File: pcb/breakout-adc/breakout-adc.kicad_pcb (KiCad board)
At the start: 4 copper layers, 100 x 62 mm, 107 parts, among them J1 Screw_Terminal_01x04, J10 Conn_01x01_Pin, J11 Conn_01x12_Pin, J12 Conn_01x12_Pin, J13 Conn_01x01_Pin, J14 Conn_01x01_Pin, J15 FX18-120P-0.8SV20, J16 Conn_01x01_Pin, J17 Conn_01x01_Pin, J18 Conn_01x01_Pin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

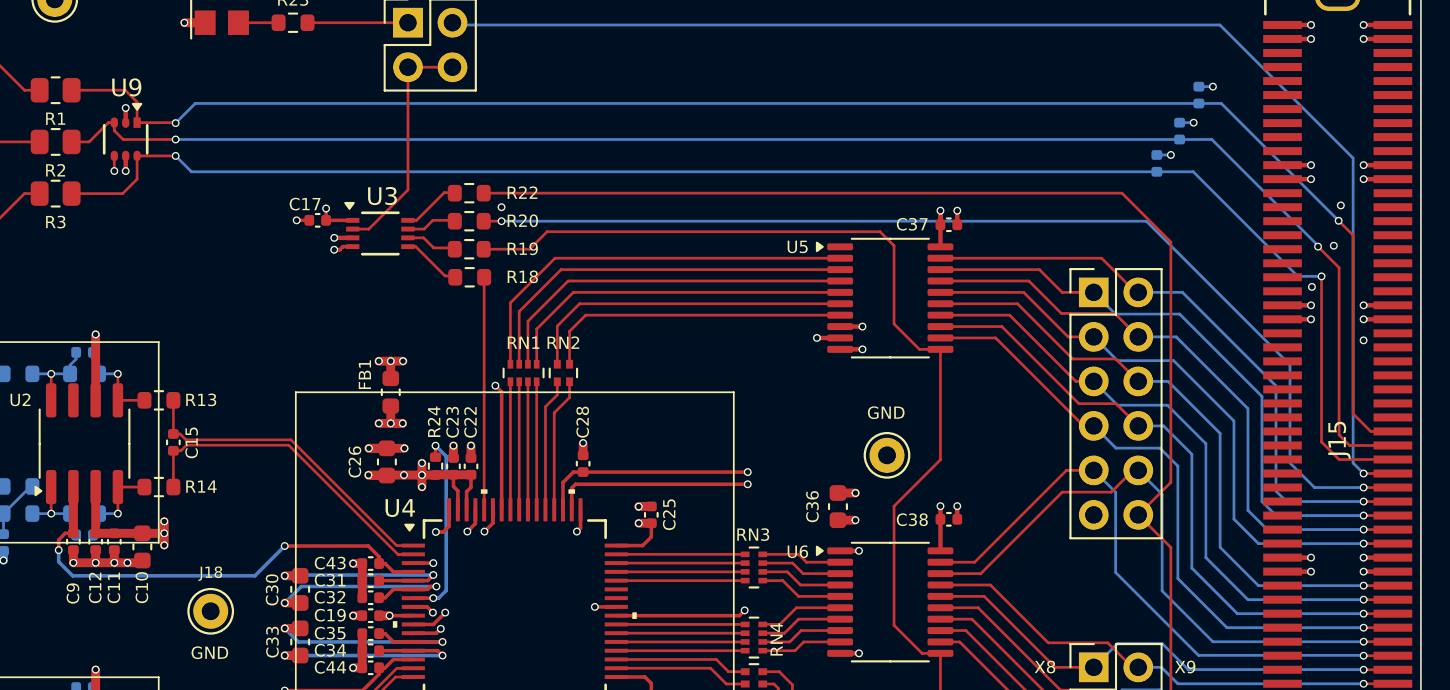
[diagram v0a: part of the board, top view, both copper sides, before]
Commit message: [adc][pcb] silk screen touch ups
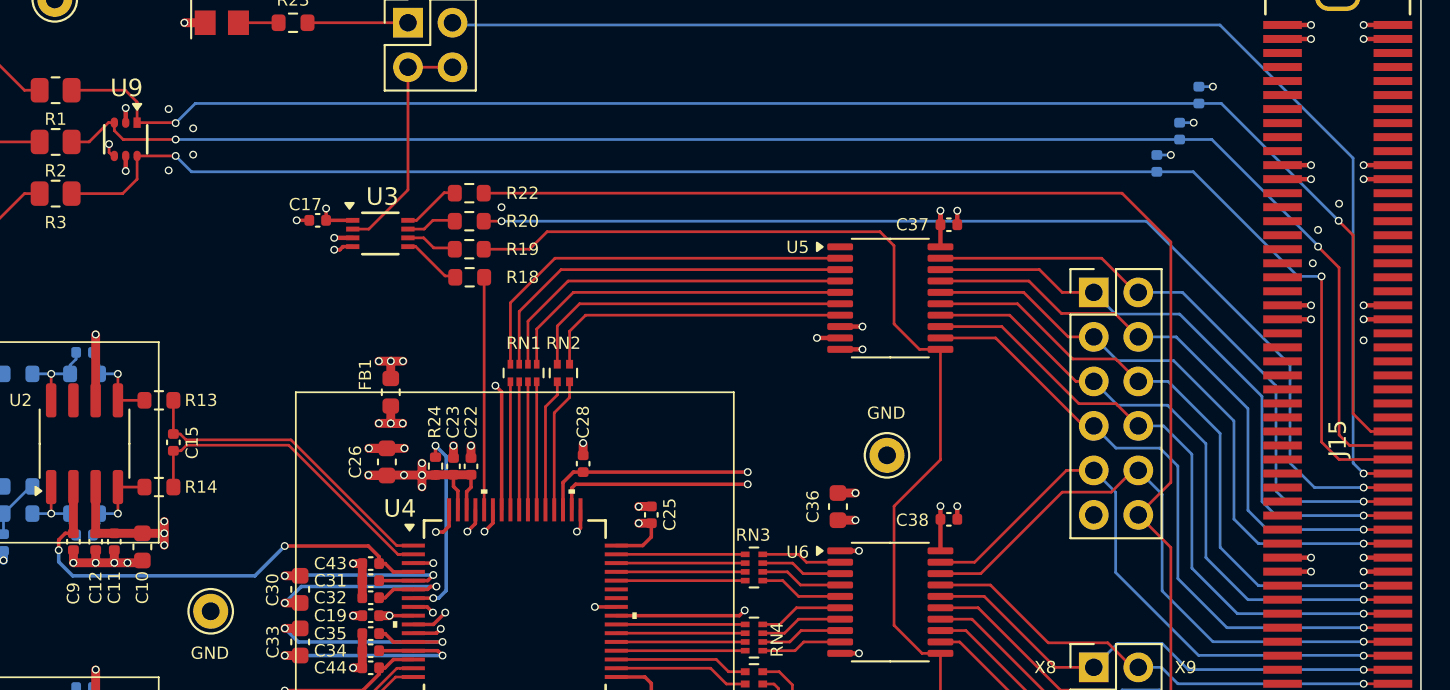
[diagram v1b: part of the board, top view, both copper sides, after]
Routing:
- net GND: track 148.8 -> 148.9 mm, vias 88 -> 92
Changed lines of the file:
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@@
 		)
 		(fp_line
-			(start -1.33 1.270001)
+			(start -1.33 1.27)
 			(end -1.33 14.03)
 			(stroke
@@
 		)
 		(fp_line
-			(start -1.33 1.270001)
+			(start -1.33 1.27)
 			(end 1.27 1.27)
 			(stroke
@@
 		)
 		(fp_line
-			(start 1.27 1.27)
-			(end 1.270001 -1.33)
+			(start 1.27 -1.33)
+			(end 3.87 -1.33)
 			(stroke
 				(width 0.12)
@@
 		)
 		(fp_line
-			(start 1.270001 -1.33)
-			(end 3.87 -1.33)
+			(start 1.27 1.27)
+			(end 1.27 -1.33)
 			(stroke
 				(width 0.12)
@@
 		)
 		(fp_line
-			(start -1.270001 0)
-			(end 0 -1.270001)
+			(start -1.27 0)
+			(end 0 -1.27)
 			(stroke
 				(width 0.1)
@@
 		(fp_line
 			(start -1.27 13.97)
-			(end -1.270001 0)
+			(end -1.27 0)
 			(stroke
 				(width 0.1)
@@
 		)
 		(fp_line
-			(start 0 -1.270001)
+			(start 0 -1.27)
 			(end 3.81 -1.27)
 			(stroke
@@
 		)
 		(pad "5" thru_hole oval
-			(at 0 5.079999)
+			(at 0 5.08)
 			(size 1.7 1.7)
 			(drill 1)
@@
 			(at 0.032 -2.2064 0)
 			(layer "F.SilkS")
+			(hide yes)
 			(effects
 				(font
@@
 		)
 		(fp_line
-			(start -1.33 1.270001)
+			(start -1.33 1.27)
 			(end -1.33 14.03)
 			(stroke
@@
 		)
 		(fp_line
-			(start -1.33 1.270001)
+			(start -1.33 1.27)
 			(end 1.27 1.27)
 			(stroke
@@
 		)
 		(fp_line
-			(start 1.27 1.27)
-			(end 1.270001 -1.33)
+			(start 1.27 -1.33)
+			(end 3.87 -1.33)
 			(stroke
 				(width 0.12)
@@
 		)
 		(fp_line
-			(start 1.270001 -1.33)
-			(end 3.87 -1.33)
+			(start 1.27 1.27)
+			(end 1.27 -1.33)
 			(stroke
 				(width 0.12)
@@
 		)
 		(fp_line
-			(start -1.270001 0)
-			(end 0 -1.270001)
+			(start -1.27 0)
+			(end 0 -1.27)
 			(stroke
 				(width 0.1)
@@
 		(fp_line
 			(start -1.27 13.97)
-			(end -1.270001 0)
+			(end -1.27 0)
 			(stroke
 				(width 0.1)
@@
 		)
 		(fp_line
-			(start 0 -1.270001)
+			(start 0 -1.27)
 			(end 3.81 -1.27)
 			(stroke
@@
 		)
 		(pad "5" thru_hole oval
-			(at 0 5.079999)
+			(at 0 5.08)
 			(size 1.7 1.7)
 			(drill 1)
@@
 	)
 	(segment
-		(start 134.100002 58.775003)
-		(end 134.100002 59.536974)
-		(width 0.156464)
-		(layer "F.Cu")
-		(net 1)
-	)
-	(segment
 		(start 154.456667 94.113025)
 		(end 154.456666 94.113026)
@@
 	)
 	(segment
+		(start 133.8 58)
+		(end 133.8 58.475001)
+		(width 0.156464)
+		(layer "F.Cu")
+		(net 1)
+	)
+	(segment
 		(start 176.55 81.213026)
 		(end 176.6 81.263026)
@@
 	)
 	(segment
+		(start 133.8 58.475001)
+		(end 134.100002 58.775003)
+		(width 0.156464)
+		(layer "F.Cu")
+		(net 1)
+	)
+	(segment
 		(start 152.986469 84.738026)
 		(end 152.311468 85.413027)
@@
 	)
 	(via
-		(at 134.100002 59.536974)
+		(at 133.8 58)
 		(size 0.45)
 		(drill 0.3)
@@
 	)
 	(via
+		(at 137.2 56)
+		(size 0.45)
+		(drill 0.3)
+		(layers "F.Cu" "B.Cu")
+		(net 1)
+	)
+	(via
 		(at 202.4 51.2)
 		(size 0.45)
@@
 	)
 	(via
-		(at 204.1 61.5)
+		(at 204 61.4)
 		(size 0.45)
 		(drill 0.3)
@@
 	)
 	(via
-		(at 202.45 66.15)
+		(at 202.5 64.8)
 		(size 0.45)
 		(drill 0.3)
@@
 	)
 	(via
+		(at 138.6 57.1)
+		(size 0.45)
+		(drill 0.3)
+		(layers "F.Cu" "B.Cu")
+		(net 1)
+	)
+	(via
 		(at 127.775 100.885693)
 		(size 0.45)
@@
 	)
 	(via
+		(at 137.2 59.5)
+		(size 0.45)
+		(drill 0.3)
+		(layers "F.Cu" "B.Cu")
+		(net 1)
+	)
+	(via
 		(at 170.25 91.758223)
 		(size 0.45)
@@
 	)
 	(via
-		(at 203.7 63.8)
+		(at 202.8 62.9)
 		(size 0.45)
 		(drill 0.3)
@@
 		(size 0.45)
 		(drill 0.3)
+		(layers "F.Cu" "B.Cu")
+		(net 1)
+	)
+	(via
+		(at 138.6 58.6)
+		(size 0.45)
+		(drill 0.3)

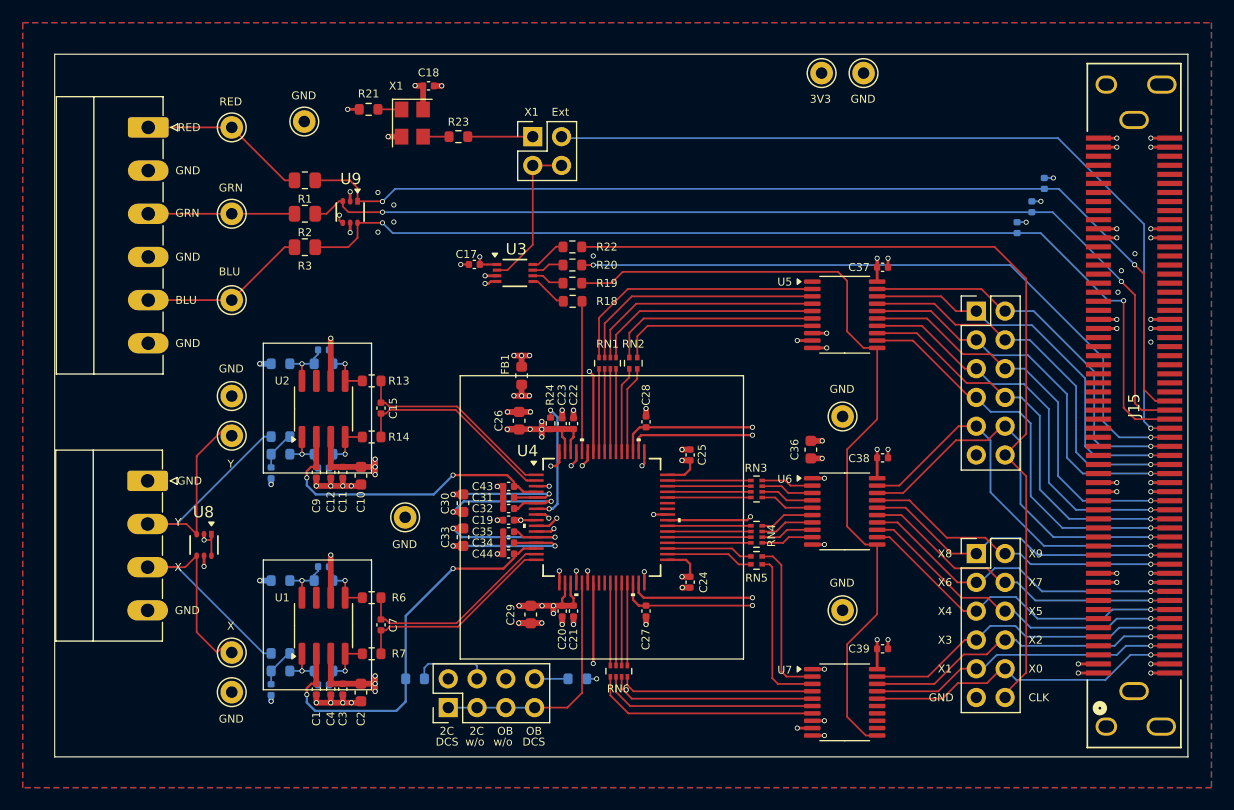
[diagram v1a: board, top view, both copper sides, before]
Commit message: [adc][pcb] add fence vias around pcb
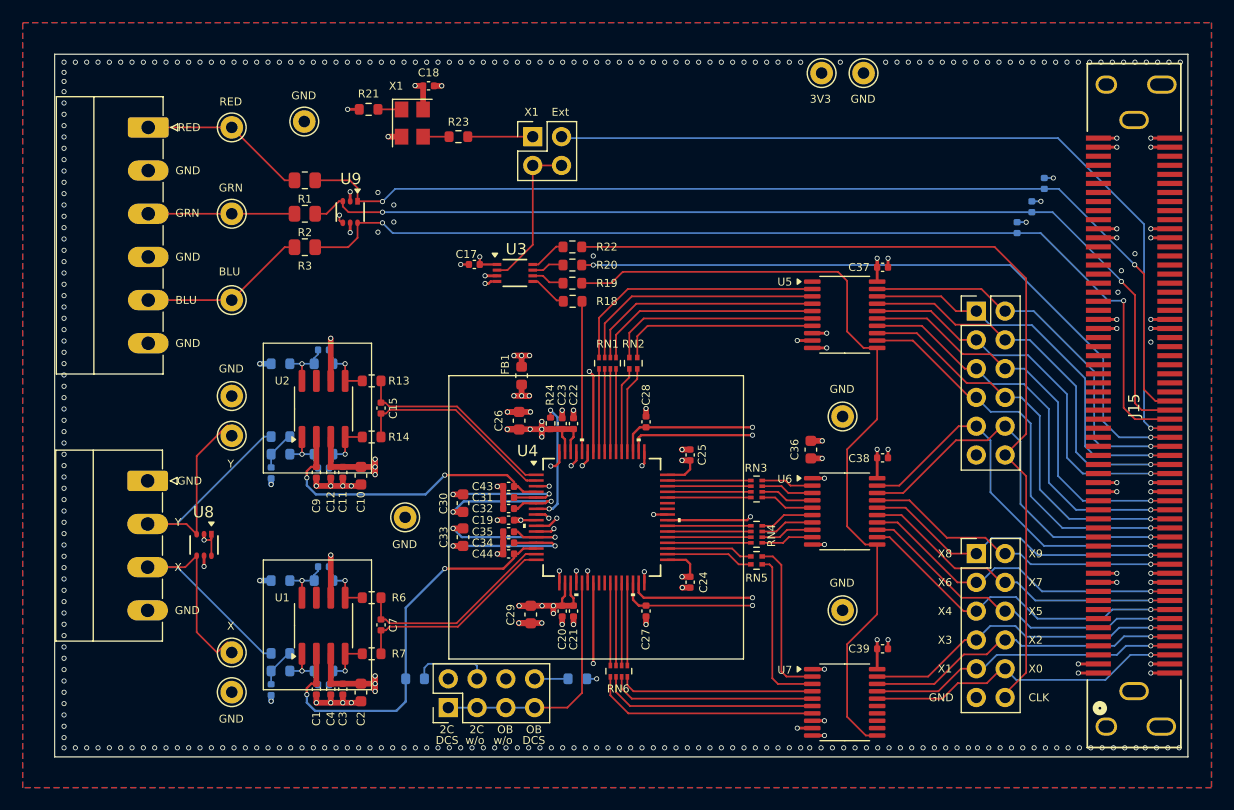
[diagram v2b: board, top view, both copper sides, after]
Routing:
- net GND: vias 92 -> 346

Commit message: [adc][pcb] replace deleted Y hdr silks
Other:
- board text added: "Y0"
- board text added: "Y1"
- board text added: "Y2"
- board text added: "Y3"
- board text added: "Y4"
- board text added: "Y5"
- board text added: "Y6"
- board text added: "Y7"
- board text added: "Y8"
- board text added: "Y9"
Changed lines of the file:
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@@
+		)
+	)
+	(gr_text "Y0"
+		(at 194.6 77.038026 0)
+		(layer "F.SilkS")
+		(effects
+			(font
+				(size 0.7 0.7)
+				(thickness 0.1)
+			)
+			(justify left bottom)
 		)
 	)
@@
 		)
 	)
+	(gr_text "Y7"
+		(at 194.6 69.418026 0)
+		(layer "F.SilkS")
+		(effects
+			(font
+				(size 0.7 0.7)
+				(thickness 0.1)
+			)
+			(justify left bottom)
+		)
+	)
 	(gr_text "Y"
 		(at 119.275 85.513026 0)
@@
 		)
 	)
+	(gr_text "GND"
+		(at 185.8 79.578026 0)
+		(layer "F.SilkS")
+		(effects
+			(font
+				(size 0.7 0.7)
+				(thickness 0.1)
+			)
+			(justify left bottom)
+		)
+	)
 	(gr_text "GRN"
 		(at 123.153334 56 0)
@@
 		)
 	)
+	(gr_text "CLK"
+		(at 194.6 79.578026 0)
+		(layer "F.SilkS")
+		(effects
+			(font
+				(size 0.7 0.7)
+				(thickness 0.1)
+			)
+			(justify left bottom)
+		)
+	)
 	(gr_text "X6"
 		(at 186.599999 90.818026 0)
@@
 		)
 	)
+	(gr_text "Y9"
+		(at 194.6 66.878026 0)
+		(layer "F.SilkS")
+		(effects
+			(font
+				(size 0.7 0.7)
+				(thickness 0.1)
+			)
+			(justify left bottom)
+		)
+	)
 	(gr_text "GND"
 		(at 119.275 93.288026 0)
@@
 		)
 	)
+	(gr_text "Y5"
+		(at 194.6 71.958026 0)
+		(layer "F.SilkS")
+		(effects
+			(font
+				(size 0.7 0.7)
+				(thickness 0.1)
+			)
+			(justify left bottom)
+		)
+	)
 	(gr_text "BLU"
 		(at 123.153334 63.4 0)
@@
 		)
 	)
+	(gr_text "Y4"
+		(at 186.599999 71.958026 0)
+		(layer "F.SilkS")
+		(effects
+			(font
+				(size 0.7 0.7)
+				(thickness 0.1)
+			)
+			(justify left bottom)
+		)
+	)
 	(gr_text "RED"
 		(at 119.5325 50.67 0)
@@
 		)
 	)
+	(gr_text "Y6"
+		(at 186.599999 69.418026 0)
+		(layer "F.SilkS")
+		(effects
+			(font
+				(size 0.7 0.7)
+				(thickness 0.1)
+			)
+			(justify left bottom)
+		)
+	)
 	(gr_text "X5"
 		(at 194.6 93.358026 0)
@@
 		)
 	)
+	(gr_text "Y3"
+		(at 194.6 74.498026 0)
+		(layer "F.SilkS")
+		(effects
+			(font
+				(size 0.7 0.7)
+				(thickness 0.1)
+			)
+			(justify left bottom)
+		)
+	)
 	(gr_text "GND"
 		(at 129.553334 47.863026 0)
@@
 		)
 	)
+	(gr_text "Y2"
+		(at 186.599999 74.498026 0)
+		(layer "F.SilkS")
+		(effects
+			(font
+				(size 0.7 0.7)
+				(thickness 0.1)
+			)
+			(justify left bottom)
+		)
+	)
 	(gr_text "X1"
 		(at 150.113333 49.313026 0)
 		(layer "F.SilkS")
 		(effects
+			(font
+				(size 0.7 0.7)
+				(thickness 0.1)
+			)
+			(justify left bottom)
+		)
+	)
+	(gr_text "Y8"
+		(at 186.599999 66.878026 0)
+		(layer "F.SilkS")
+		(effects
+			(font
+				(size 0.7 0.7)
+				(thickness 0.1)
+			)
+			(justify left bottom)
+		)
+	)
+	(gr_text "Y1"
+		(at 186.599999 77.038026 0)
+		(layer "F.SilkS")
+		(effects

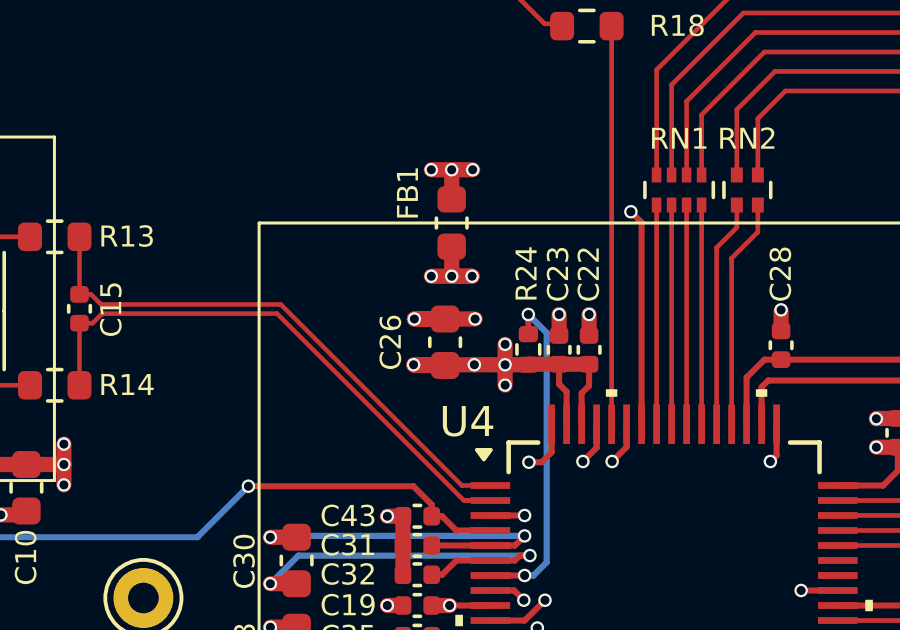
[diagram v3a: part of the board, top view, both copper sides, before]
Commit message: [adc][pcb] add remaining part numbers
missing test points for lcsc, but otherwise done
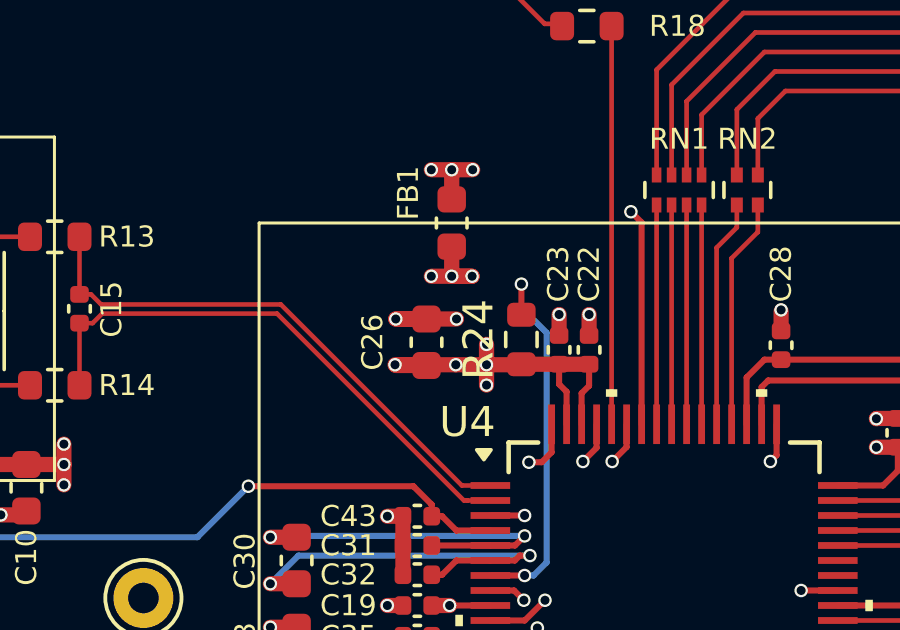
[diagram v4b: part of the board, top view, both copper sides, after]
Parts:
- J10, J14, J16, J17, J18, J5, J6: value Conn_01x01_Pin -> Black
- J11, J12: value Conn_01x12_Pin -> Conn_02x06_Pin
- J13, J7: value Conn_01x01_Pin -> Red
- J2: value Screw_Terminal_01x02 -> Screw_Terminal_01x06
- J3, J4: value Conn_01x01_Pin -> White
- J8: value Conn_01x01_Pin -> Green
- J9: value Conn_01x01_Pin -> Blue
- R12: value 1.8k -> 1.82k
- R15, R16: value 900 -> 910
- R24: footprint Resistor_SMD:R_0402_1005Metric -> Resistor_SMD:R_0603_1608Metric
- moved C26 0.62 mm to (149.0, 76.1)
- moved R24 0.40 mm to (152.2, 76.0)
